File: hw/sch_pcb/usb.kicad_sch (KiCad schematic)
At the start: 0 parts

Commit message: Schematics structure change.
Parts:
- added C45, C48: 100nF, Capacitor_SMD:C_0603_1608Metric, symbol Device:C
- added D3, D4: YELLOW, LED_SMD:LED_1206_3216Metric, symbol Device:LED
- added J4: USBC_USB4105-GF-A, Mlab_CON:USBC GCT_USB4105-GF-A, symbol MLAB_CONNECTORS:USBC_USB4105-GF-A
- added R26: 4k7, Resistor_SMD:R_0603_1608Metric, symbol Device:R
- added R27: 10k, Resistor_SMD:R_0603_1608Metric, symbol Device:R
- added R28, R29: 180R, Resistor_SMD:R_0603_1608Metric, symbol Device:R
- added R30, R31: 5k1, Resistor_SMD:R_0603_1608Metric, symbol Device:R
- added U7: USBLC6-2SC6, Package_TO_SOT_SMD:SOT-23-6, symbol Power_Protection:USBLC6-2SC6
- added U9: FT231XQ, Package_DFN_QFN:QFN-20-1EP_4x4mm_P0.5mm_EP2.5x2.5mm, symbol Interface_USB:FT231XQ
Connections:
- new net: R26.2, R27.1, U9.11 (~{RESET})
- new net: D4.1 (K), R29.1
- new net: D3.1 (K), R28.1
- new net: J4.B5 (CC2), R31.1
- new net: J4.A5 (CC1), R30.1
- new net +3V3: C45.1, C48.1, D3.2 (A), D4.2 (A), U9.10 (3V3OUT), U9.12 (VCC), U9.20 (VCCIO)
- new net D+: J4.A6 (D+), J4.B6 (D+), U7.4 (I/O2)
- new net D-: J4.A7 (D-), J4.B7 (D-), U7.6 (I/O1)
- new net DM: U7.1 (I/O1), U9.9 (USBDM)
- new net DP: U7.3 (I/O2), U9.8 (USBDP)
- new net GND: C45.2, C48.2, J4.A1/B12 (GND), J4.B1/A12 (GND), J4.G1 (SHIELD), J4.G2 (SHIELD), J4.G3 (SHIELD), J4.G4 (SHIELD), R27.2, R30.2, R31.2, U7.2 (GND), U9.13 (GND), U9.21 (GND), U9.3 (GND)
- new net RST#: U9.18 (~{DTR})
- new net RX0: U9.17 (TXD)
- new net RXLED/CBUS1: R29.2, U9.14 (CBUS1)
- new net TX0: U9.1 (RXD)
- new net TXLED/CBUS2: R28.2, U9.7 (CBUS2)
- new net VBUS: J4.A4/B9 (VBUS), J4.B4/A9 (VBUS), R26.1, U7.5 (VBUS)
- no-connect marks 0 -> 9
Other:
- note added: "CBUS Defaults CBUS0 - TXDEN CBUS1 - RXLED CBUS2 - TXLED CBUS3 - SLEEP#"

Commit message: Schematics cleanup of power symbols and routing.
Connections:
- net VBUS: no longer J4.A4/B9 (VBUS), J4.B4/A9 (VBUS), R26.1
- new net VUSB: J4.A4/B9 (VBUS), J4.B4/A9 (VBUS), R26.1
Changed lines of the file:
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@@
   (junction (at 151.13 73.66) (diameter 0) (color 0 0 0 0)
+  )
+  (junction (at 64.77 52.07) (diameter 0) (color 0 0 0 0)
   )
   (no_connect (at 166.37 100.33))
@@
   (no_connect (at 166.37 107.95))
   (no_connect (at 58.42 82.55))
+  (wire (pts (xy 64.77 52.07) (xy 64.77 48.26))
+    (stroke (width 0) (type default) (color 0 0 0 0))
+  )
   (wire (pts (xy 36.83 119.38) (xy 39.37 119.38))
     (stroke (width 0) (type solid) (color 0 0 0 0))
@@
     (stroke (width 0) (type solid) (color 0 0 0 0))
   )
-  (wire (pts (xy 58.42 52.07) (xy 60.96 52.07))
+  (wire (pts (xy 58.42 52.07) (xy 64.77 52.07))
     (stroke (width 0) (type solid) (color 0 0 0 0))
   )
@@
   (wire (pts (xy 67.31 57.15) (xy 71.12 57.15))
     (stroke (width 0) (type solid) (color 0 0 0 0))
+  )
+  (wire (pts (xy 64.77 52.07) (xy 71.12 52.07))
+    (stroke (width 0) (type default) (color 0 0 0 0))
   )
   (wire (pts (xy 166.37 105.41) (xy 179.07 105.41))
@@
     (effects (font (size 1.27 1.27)) (justify right bottom))
   )
-  (label "VBUS" (at 60.96 52.07 0)
-    (effects (font (size 1.524 1.524)) (justify left bottom))
-  )
   (label "TXLED{slash}CBUS2" (at 229.87 107.95 270)
     (effects (font (size 1.27 1.27)) (justify right bottom))
@@
     (effects (font (size 1.27 1.27)) (justify right bottom))
   )
-  (label "VBUS" (at 102.87 95.25 180)
+  (label "VUSB" (at 102.87 95.25 180)
     (effects (font (size 1.27 1.27)) (justify right bottom))
   )
@@
   (label "D+" (at 68.58 71.12 0)
     (effects (font (size 1.524 1.524)) (justify left bottom))
+  )
+  (label "VUSB" (at 71.12 52.07 180)
+    (effects (font (size 1.27 1.27)) (justify right bottom))
   )
   (label "D-" (at 68.58 66.04 0)
@@
     )
   )
+  (hierarchical_label "VUSB" (shape input) (at 64.77 48.26 90)
+    (effects (font (size 1.524 1.524)) (justify left))
+  )
   (symbol (lib_id "Device:R") (at 102.87 116.84 0) (unit 1)

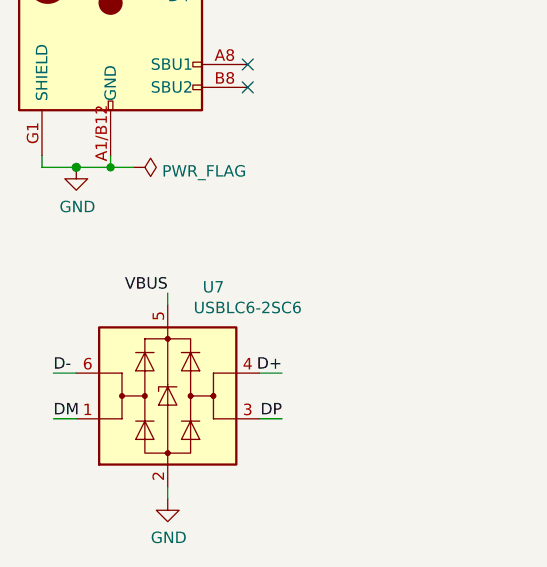
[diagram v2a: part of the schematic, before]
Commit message: Cleanup schematics Note polarity to ceramic capacitors.
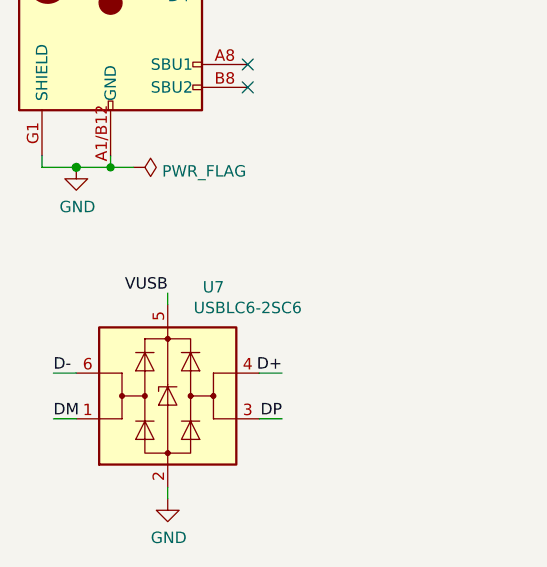
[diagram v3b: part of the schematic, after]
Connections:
- net VBUS is gone; now on net VUSB: U7.5 (VBUS)
- net +3V3 renamed +3.3V
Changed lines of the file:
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@@
     (effects (font (size 1.27 1.27)) (justify right bottom))
   )
-  (label "VBUS" (at 49.53 105.41 180)
+  (label "VUSB" (at 49.53 105.41 180)
     (effects (font (size 1.27 1.27)) (justify right bottom))
   )

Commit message: Changed voltage reference to 0.9V.
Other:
- company: (none) -> UST.cz
- title: (none) -> USTSIPIN02A
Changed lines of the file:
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@@
 (kicad_sch (version 20211123) (generator eeschema)
   (paper "A4")
+  (title_block
+    (title "USTSIPIN02A")
+    (date "2022-05-22")
+    (company "UST.cz")
+    (comment 2 "Silicon PIN diode based\\ndosimeter and spectrometer")
+    (comment 3 "info@ust.cz")
+  )
   (junction (at 67.31 66.04) (diameter 1.016) (color 0 0 0 0)
   )

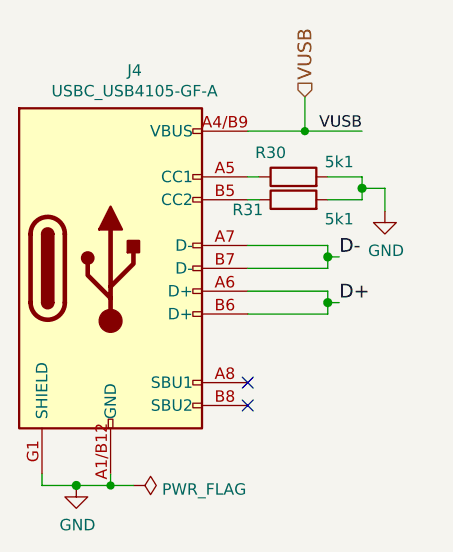
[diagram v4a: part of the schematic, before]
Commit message: Update UST_ID for voltage regulator.
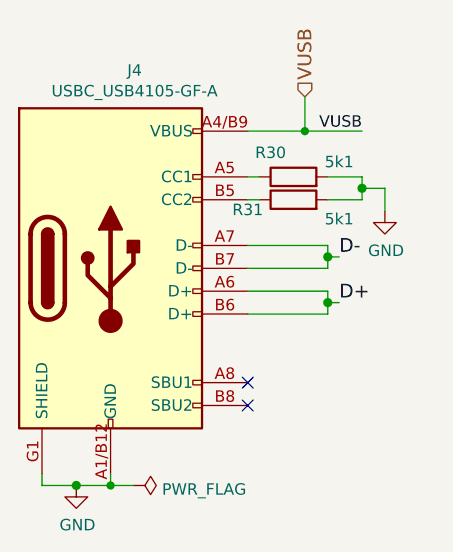
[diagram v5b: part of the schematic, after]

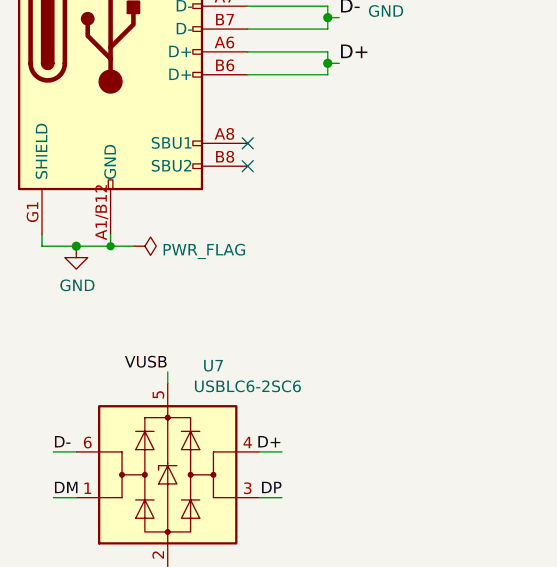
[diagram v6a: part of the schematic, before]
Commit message: Add filtering capacitor to 5V voltage supply.
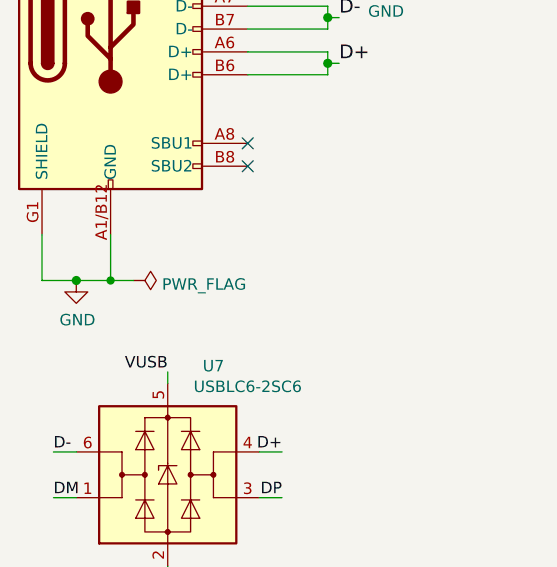
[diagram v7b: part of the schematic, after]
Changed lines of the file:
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@@
   (junction (at 67.31 66.04) (diameter 1.016) (color 0 0 0 0)
   )
-  (junction (at 43.18 91.44) (diameter 0) (color 0 0 0 0)
-  )
-  (junction (at 39.37 91.44) (diameter 1.016) (color 0 0 0 0)
+  (junction (at 43.18 95.25) (diameter 0) (color 0 0 0 0)
+  )
+  (junction (at 39.37 95.25) (diameter 1.016) (color 0 0 0 0)
   )
   (junction (at 102.87 110.49) (diameter 1.016) (color 0 0 0 0)
@@
     (stroke (width 0) (type default))
   )
-  (wire (pts (xy 35.56 90.17) (xy 35.56 91.44))
+  (wire (pts (xy 35.56 90.17) (xy 35.56 95.25))
     (stroke (width 0) (type solid))
   )
@@
     (stroke (width 0) (type default))
   )
-  (wire (pts (xy 43.18 91.44) (xy 45.72 91.44))
+  (wire (pts (xy 43.18 95.25) (xy 45.72 95.25))
     (stroke (width 0) (type default))
   )
@@
     (stroke (width 0) (type solid))
   )
+  (wire (pts (xy 43.18 90.17) (xy 43.18 95.25))
+    (stroke (width 0) (type solid))
+  )
   (wire (pts (xy 49.53 105.41) (xy 49.53 106.68))
     (stroke (width 0) (type solid))
   )
-  (wire (pts (xy 43.18 91.44) (xy 43.18 90.17))
-    (stroke (width 0) (type solid))
-  )
   (wire (pts (xy 128.27 105.41) (xy 130.81 105.41))
     (stroke (width 0) (type solid))
@@
     (stroke (width 0) (type default))
   )
-  (wire (pts (xy 35.56 91.44) (xy 39.37 91.44))
+  (wire (pts (xy 35.56 95.25) (xy 39.37 95.25))
     (stroke (width 0) (type solid))
   )
@@
     (stroke (width 0) (type solid))
   )
-  (wire (pts (xy 39.37 91.44) (xy 43.18 91.44))
+  (wire (pts (xy 39.37 95.25) (xy 43.18 95.25))
     (stroke (width 0) (type solid))
   )
@@
     )
   )
-  (symbol (lib_id "power:PWR_FLAG") (at 45.72 91.44 270) (unit 1)
+  (symbol (lib_id "power:PWR_FLAG") (at 45.72 95.25 270) (unit 1)
     (in_bom yes) (on_board yes) (dnp no) (fields_autoplaced)
-    (property "Reference" "#FLG0110" (at 47.625 91.44 0)
-      (effects (font (size 1.27 1.27)) hide)
-    )
-    (property "Value" "PWR_FLAG" (at 48.895 91.8738 90)
+    (property "Reference" "#FLG0110" (at 47.625 95.25 0)
+      (effects (font (size 1.27 1.27)) hide)
+    )
+    (property "Value" "PWR_FLAG" (at 48.895 95.6838 90)
       (effects (font (size 1.27 1.27)) (justify left))
     )
-    (property "Footprint" "" (at 45.72 91.44 0)
-      (effects (font (size 1.27 1.27)) hide)
-    )
-    (property "Datasheet" "~" (at 45.72 91.44 0)
+    (property "Footprint" "" (at 45.72 95.25 0)
+      (effects (font (size 1.27 1.27)) hide)
+    )
+    (property "Datasheet" "~" (at 45.72 95.25 0)
       (effects (font (size 1.27 1.27)) hide)
     )
@@
     )
   )
-  (symbol (lib_id "power:GND") (at 39.37 91.44 0) (unit 1)
-    (in_bom yes) (on_board yes) (dnp no)
-    (property "Reference" "#PWR0113" (at 39.37 97.79 0)
-      (effects (font (size 1.27 1.27)) hide)
-    )
-    (property "Value" "GND" (at 39.497 95.8342 0)
-      (effects (font (size 1.27 1.27)))
-    )
-    (property "Footprint" "" (at 39.37 91.44 0)
-      (effects (font (size 1.27 1.27)) hide)
-    )
-    (property "Datasheet" "" (at 39.37 91.44 0)
-      (effects (font (size 1.27 1.27)) hide)
-    )
+  (symbol (lib_id "power:GND") (at 39.37 95.25 0) (unit 1)
+    (in_bom yes) (on_board yes) (dnp no)
+    (property "Reference" "#PWR0113" (at 39.37 101.6 0)
+      (effects (font (size 1.27 1.27)) hide)
+    )
+    (property "Value" "GND" (at 39.497 99.6442 0)
+      (effects (font (size 1.27 1.27)))
+    )
+    (property "Footprint" "" (at 39.37 95.25 0)
+      (effects (font (size 1.27 1.27)) hide)
+    )
+    (property "Datasheet" "" (at 39.37 95.25 0)
+      (effects (font (size 1.27 1.27)) hide)
+    )

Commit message: Switch of most passive components to 0805 size.
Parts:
- C45, C48: footprint Capacitor_SMD:C_0603_1608Metric -> Capacitor_SMD:C_0805_2012Metric
- R26, R27, R28, R29, R30, R31: footprint Resistor_SMD:R_0603_1608Metric -> Resistor_SMD:R_0805_2012Metric
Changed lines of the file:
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@@
       (effects (font (size 1.27 1.27)) (justify left))
     )
-    (property "Footprint" "Resistor_SMD:R_0603_1608Metric" (at 101.092 116.84 90)
+    (property "Footprint" "Resistor_SMD:R_0805_2012Metric" (at 101.092 116.84 90)
       (effects (font (size 1.27 1.27)) hide)
     )
@@
       (effects (font (size 1.27 1.27)) (justify left))
     )
-    (property "Footprint" "Resistor_SMD:R_0603_1608Metric" (at 240.792 101.6 90)
+    (property "Footprint" "Resistor_SMD:R_0805_2012Metric" (at 240.792 101.6 90)
       (effects (font (size 1.27 1.27)) hide)
     )
@@
       (effects (font (size 1.27 1.27)) (justify left))
     )
-    (property "Footprint" "Resistor_SMD:R_0603_1608Metric" (at 228.092 101.6 90)
+    (property "Footprint" "Resistor_SMD:R_0805_2012Metric" (at 228.092 101.6 90)
       (effects (font (size 1.27 1.27)) hide)
     )
@@
       (effects (font (size 1.27 1.27)) (justify left))
     )
-    (property "Footprint" "Capacitor_SMD:C_0603_1608Metric" (at 160.9852 82.55 0)
+    (property "Footprint" "Capacitor_SMD:C_0805_2012Metric" (at 160.9852 82.55 0)
       (effects (font (size 1.27 1.27)) hide)
     )
@@
       (effects (font (size 1.27 1.27)))
     )
-    (property "Footprint" "Resistor_SMD:R_0603_1608Metric" (at 63.5 61.468 90)
+    (property "Footprint" "Resistor_SMD:R_0805_2012Metric" (at 63.5 61.468 90)
       (effects (font (size 1.27 1.27)) hide)
     )
@@
       (effects (font (size 1.27 1.27)))
     )
-    (property "Footprint" "Resistor_SMD:R_0603_1608Metric" (at 63.5 58.928 90)
+    (property "Footprint" "Resistor_SMD:R_0805_2012Metric" (at 63.5 58.928 90)
       (effects (font (size 1.27 1.27)) hide)
     )
@@
       (effects (font (size 1.27 1.27)) (justify left))
     )
-    (property "Footprint" "Capacitor_SMD:C_0603_1608Metric" (at 115.2652 102.87 0)
+    (property "Footprint" "Capacitor_SMD:C_0805_2012Metric" (at 115.2652 102.87 0)
       (effects (font (size 1.27 1.27)) hide)
     )
@@
       (effects (font (size 1.27 1.27)) (justify left))
     )
-    (property "Footprint" "Resistor_SMD:R_0603_1608Metric" (at 101.092 104.14 90)
-      (effects (font (size 1.27 1.27)) hide)
-    )
+    (property "Footprint" "Resistor_SMD:R_0805_2012Metric" (at 101.092 104.14 90)
+      (effects (font (size 1.27 1.27)) hide)
+    )
